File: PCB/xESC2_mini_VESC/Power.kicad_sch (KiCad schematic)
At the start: 20 parts, among them J10 Conn_01x06_Male, J9 Conn_01x06_Male, U1 TMC6200-TA

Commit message: BoM data updates
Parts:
- C12, C13, C14: Config (none) -> use the 603 in next rev; Digikey use the 603 in next rev -> (none); Part Number (none) -> HMK212BJ104KG-T
- J10, J9: LCSC (none) -> C2935912; Part Number (none) -> DZ254R-11-06-63; Stock_PN (none) -> J-TH-1x6-.1
- R13: Config (none) -> do not place
- R14, R15, R29: Digikey RC0603FR-0710KL -> 311-10.0KHRCT-ND; Part Number 311-10.0KHRCT-ND -> RC0603FR-0710KL
- R16: Digikey RC0603FR-07150RL -> 311-150HRCT-ND; Part Number 311-150HRCT-ND -> RC0603FR-07150RL
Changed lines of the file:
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@@
       (effects (font (size 1.27 1.27)) hide)
     )
-    (property "Digikey" "use the 603 in next rev" (id 5) (at 171.45 64.77 0)
+    (property "Digikey" "" (id 5) (at 171.45 64.77 0)
+      (effects (font (size 1.27 1.27)) hide)
+    )
+    (property "Config" "use the 603 in next rev" (id 6) (at 171.45 64.77 0)
+      (effects (font (size 1.27 1.27)) hide)
+    )
+    (property "Part Number" "HMK212BJ104KG-T" (id 7) (at 171.45 64.77 0)
       (effects (font (size 1.27 1.27)) hide)
     )
@@
       (effects (font (size 1.27 1.27)) hide)
     )
-    (property "Digikey" "use the 603 in next rev" (id 5) (at 189.23 74.93 0)
+    (property "Digikey" "" (id 5) (at 189.23 74.93 0)
+      (effects (font (size 1.27 1.27)) hide)
+    )
+    (property "Config" "use the 603 in next rev" (id 6) (at 189.23 74.93 0)
+      (effects (font (size 1.27 1.27)) hide)
+    )
+    (property "Part Number" "HMK212BJ104KG-T" (id 7) (at 189.23 74.93 0)
       (effects (font (size 1.27 1.27)) hide)
     )
@@
       (effects (font (size 1.27 1.27)) hide)
     )
+    (property "Config" "do not place" (id 4) (at 201.93 134.62 0)
+      (effects (font (size 1.27 1.27)) hide)
+    )
     (pin "1")
     (pin "2")
@@
       (effects (font (size 1.27 1.27)) hide)
     )
-    (property "Digikey" "RC0603FR-0710KL" (id 4) (at 201.93 148.59 0)
-      (effects (font (size 1.27 1.27)) hide)
-    )
-    (property "Part Number" "311-10.0KHRCT-ND" (id 5) (at 201.93 148.59 0)
+    (property "Digikey" "311-10.0KHRCT-ND" (id 4) (at 201.93 148.59 0)
+      (effects (font (size 1.27 1.27)) hide)
+    )
+    (property "Part Number" "RC0603FR-0710KL" (id 5) (at 201.93 148.59 0)
       (effects (font (size 1.27 1.27)) hide)
     )
@@
       (effects (font (size 1.27 1.27)) hide)
     )
-    (property "Digikey" "use the 603 in next rev" (id 5) (at 185.42 83.82 0)
+    (property "Digikey" "" (id 5) (at 185.42 83.82 0)
+      (effects (font (size 1.27 1.27)) hide)
+    )
+    (property "Config" "use the 603 in next rev" (id 6) (at 185.42 83.82 0)
+      (effects (font (size 1.27 1.27)) hide)
+    )
+    (property "Part Number" "HMK212BJ104KG-T" (id 7) (at 185.42 83.82 0)
       (effects (font (size 1.27 1.27)) hide)
     )
@@
       (effects (font (size 1.27 1.27)) hide)
     )
-    (property "Digikey" "RC0603FR-0710KL" (id 4) (at 210.82 134.62 0)
-      (effects (font (size 1.27 1.27)) hide)
-    )
-    (property "Part Number" "311-10.0KHRCT-ND" (id 5) (at 210.82 134.62 0)
+    (property "Digikey" "311-10.0KHRCT-ND" (id 4) (at 210.82 134.62 0)
+      (effects (font (size 1.27 1.27)) hide)
+    )
+    (property "Part Number" "RC0603FR-0710KL" (id 5) (at 210.82 134.62 0)
       (effects (font (size 1.27 1.27)) hide)
     )
@@
       (effects (font (size 1.27 1.27)) hide)
     )
-    (property "Digikey" "RC0603FR-0710KL" (id 4) (at 167.64 93.98 0)
-      (effects (font (size 1.27 1.27)) hide)
-    )
-    (property "Part Number" "311-10.0KHRCT-ND" (id 5) (at 167.64 93.98 0)
+    (property "Digikey" "311-10.0KHRCT-ND" (id 4) (at 167.64 93.98 0)
+      (effects (font (size 1.27 1.27)) hide)
+    )
+    (property "Part Number" "RC0603FR-0710KL" (id 5) (at 167.64 93.98 0)
       (effects (font (size 1.27 1.27)) hide)
     )
@@
       (effects (font (size 1.27 1.27)) hide)
     )
-    (property "Digikey" "RC0603FR-07150RL" (id 4) (at 185.42 135.89 0)
-      (effects (font (size 1.27 1.27)) hide)
-    )
-    (property "Part Number" "311-150HRCT-ND" (id 5) (at 185.42 135.89 0)
+    (property "Digikey" "311-150HRCT-ND" (id 4) (at 185.42 135.89 0)
+      (effects (font (size 1.27 1.27)) hide)
+    )
+    (property "Part Number" "RC0603FR-07150RL" (id 5) (at 185.42 135.89 0)
       (effects (font (size 1.27 1.27)) hide)
     )
@@
     (pin "1")
   )
-  (symbol (lib_id "Connector:Conn_01x06_Male") (at 21.59 140.97 0)
+  (symbol (lib_id "Connector:Conn_01x06_Male") (at 21.59 140.97 0) (unit 1)
     (in_bom yes) (on_board yes)
     (property "Reference" "J9" (id 0) (at 24.3332 131.2926 0))
@@
     )
     (property "Datasheet" "~" (id 3) (at 21.59 140.97 0)
+      (effects (font (size 1.27 1.27)) hide)
+    )
+    (property "LCSC" "C2935912" (id 4) (at 21.59 140.97 0)
+      (effects (font (size 1.27 1.27)) hide)
+    )
+    (property "Part Number" "DZ254R-11-06-63" (id 5) (at 21.59 140.97 0)
+      (effects (font (size 1.27 1.27)) hide)
+    )
+    (property "Stock_PN" "J-TH-1x6-.1" (id 6) (at 21.59 140.97 0)
       (effects (font (size 1.27 1.27)) hide)
     )
@@
     (pin "1")
   )
-  (symbol (lib_id "Connector:Conn_01x06_Male") (at 21.59 160.02 0)
+  (symbol (lib_id "Connector:Conn_01x06_Male") (at 21.59 160.02 0) (unit 1)
     (in_bom yes) (on_board yes)
     (property "Reference" "J10" (id 0) (at 24.3332 150.3426 0))
@@
       (effects (font (size 1.27 1.27)) hide)
     )
+    (property "LCSC" "C2935912" (id 4) (at 21.59 160.02 0)
+      (effects (font (size 1.27 1.27)) hide)
+    )
+    (property "Part Number" "DZ254R-11-06-63" (id 5) (at 21.59 160.02 0)
+      (effects (font (size 1.27 1.27)) hide)
+    )
+    (property "Stock_PN" "J-TH-1x6-.1" (id 6) (at 21.59 160.02 0)
+      (effects (font (size 1.27 1.27)) hide)
+    )

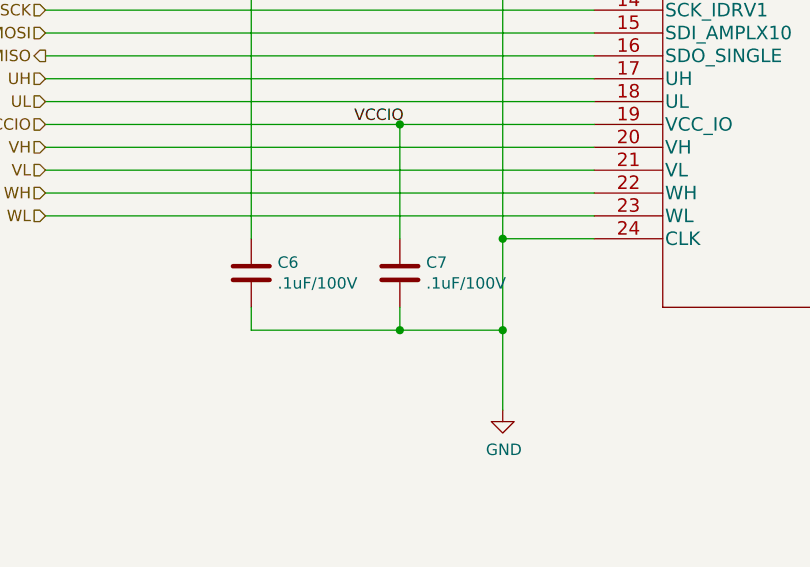
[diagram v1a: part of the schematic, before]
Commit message: updated BOM for .1uF caps
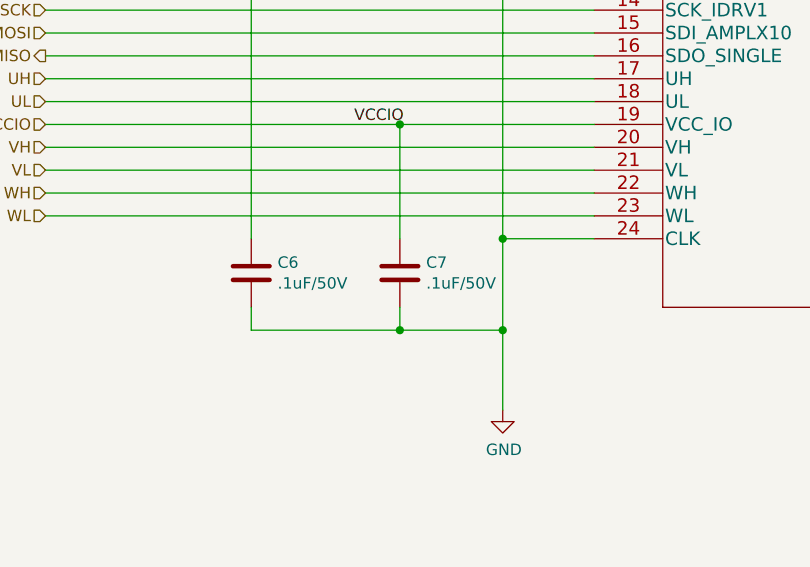
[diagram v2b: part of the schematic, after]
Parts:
- C6, C7: value .1uF/100V -> .1uF/50V; Digikey 490-1331-1-ND -> 1276-1935-1-ND
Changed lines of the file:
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@@
       (effects (font (size 1.27 1.27)) (justify left))
     )
-    (property "Value" ".1uF/100V" (id 1) (at 67.691 90.043 0)
+    (property "Value" ".1uF/50V" (id 1) (at 67.691 90.043 0)
       (effects (font (size 1.27 1.27)) (justify left))
     )
@@
       (effects (font (size 1.27 1.27)) hide)
     )
-    (property "Digikey" "490-1331-1-ND" (id 4) (at 64.77 88.9 0)
+    (property "Digikey" "1276-1935-1-ND" (id 4) (at 64.77 88.9 0)
       (effects (font (size 1.27 1.27)) hide)
     )
@@
       (effects (font (size 1.27 1.27)) (justify left))
     )
-    (property "Value" ".1uF/100V" (id 1) (at 51.181 90.043 0)
+    (property "Value" ".1uF/50V" (id 1) (at 51.181 90.043 0)
       (effects (font (size 1.27 1.27)) (justify left))
     )
@@
       (effects (font (size 1.27 1.27)) hide)
     )
-    (property "Digikey" "490-1331-1-ND" (id 4) (at 48.26 88.9 0)
+    (property "Digikey" "1276-1935-1-ND" (id 4) (at 48.26 88.9 0)
       (effects (font (size 1.27 1.27)) hide)
     )
